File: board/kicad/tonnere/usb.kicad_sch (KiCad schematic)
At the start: 30 parts, among them J19 USB_A, J20 73725-1180RLF, J24 73725-1180RLF, J25 73725-1180RLF, U36 TPD4E02B04DQA, U37 USB2514B_Bi, U38 TPD4E02B04DQA, Y8 24MHz

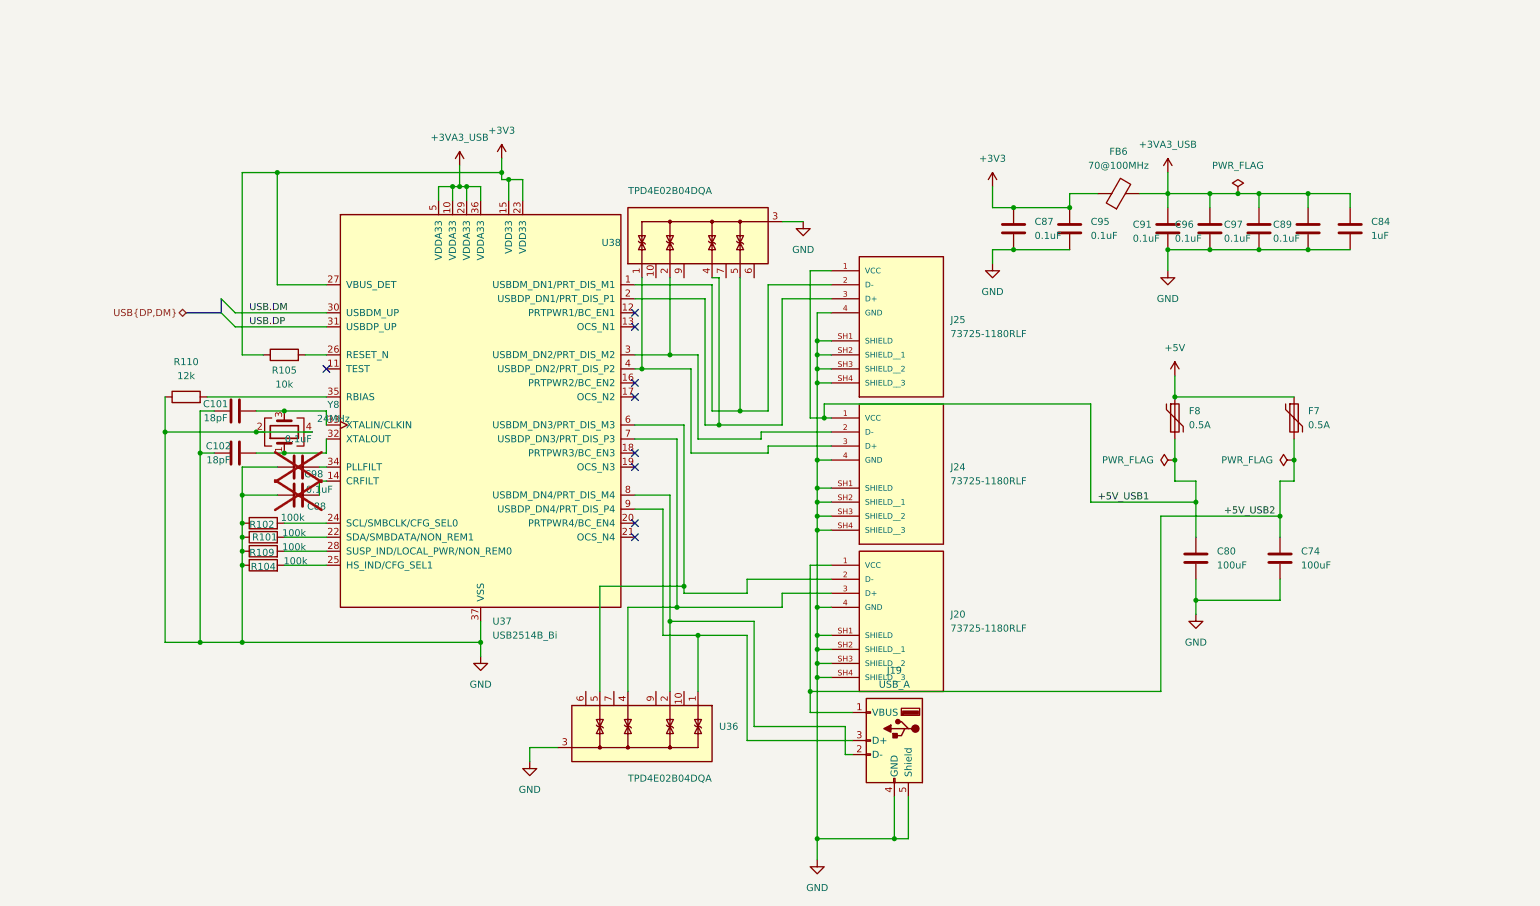
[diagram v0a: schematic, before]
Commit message: 0.60 (not final). Fix errata from 0.51. Added USB2 phy.
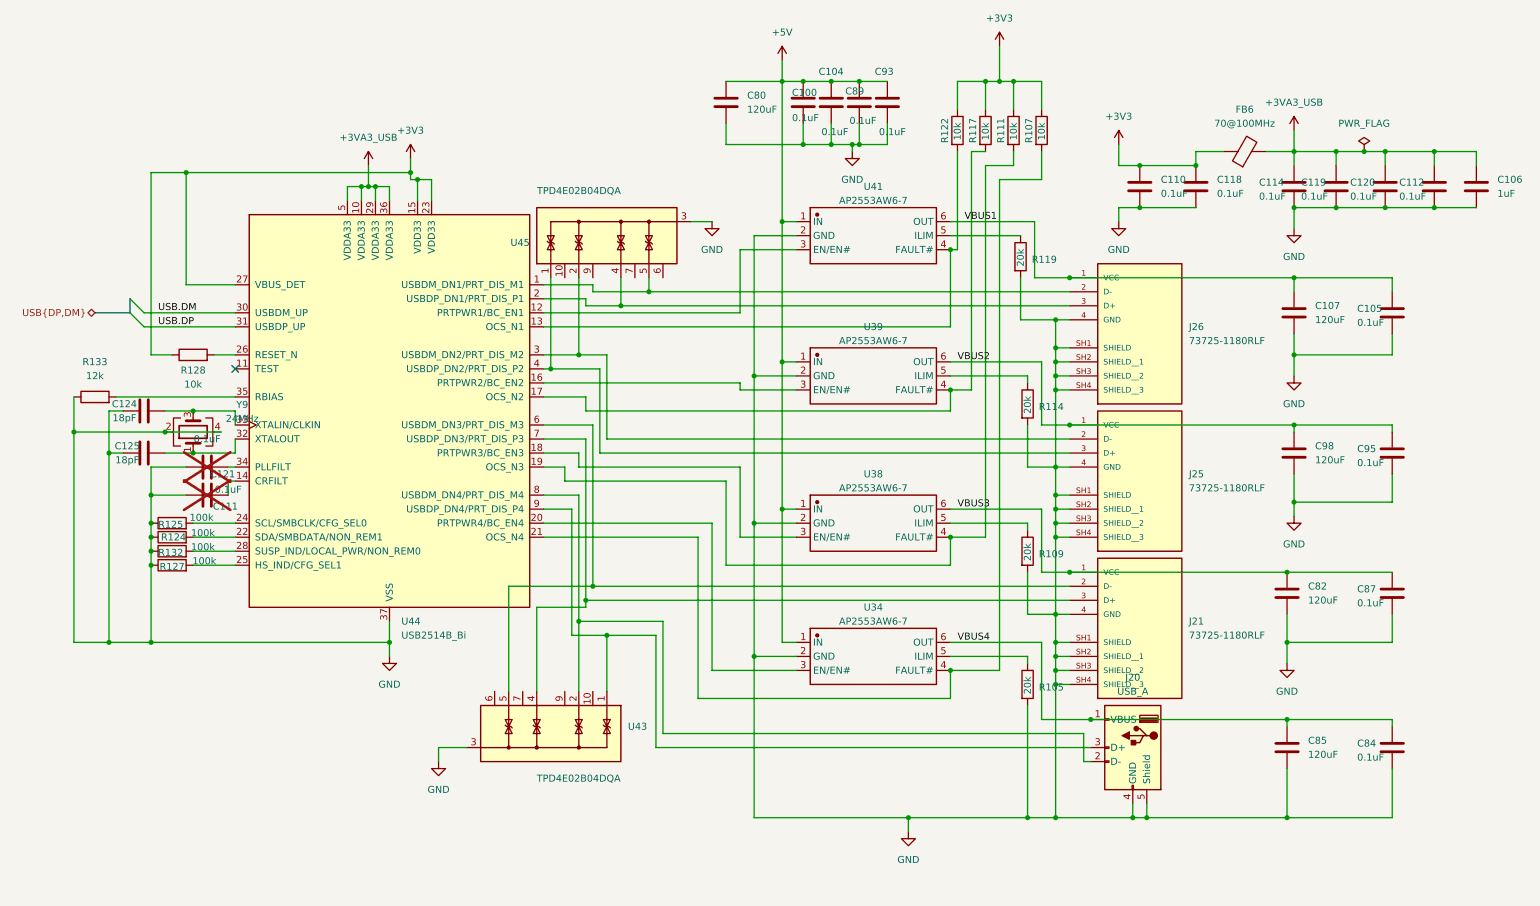
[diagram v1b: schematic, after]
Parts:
- removed C74: 100uF, Capacitor_SMD:C_1206_3216Metric, symbol Device:C
- removed F7, F8: 0.5A, Resistor_SMD:R_0603_1608Metric, symbol Device:Polyfuse
- added C100, C104, C105, C84, C87, C89, C93, C95: 0.1uF, Capacitor_SMD:C_0603_1608Metric, symbol Device:C
- added C107, C82, C85, C98: 120uF, Capacitor_SMD:C_1206_3216Metric, symbol Device:C
- added R105, R109, R114, R119: 20k, Resistor_SMD:R_0603_1608Metric, symbol Device:R
- added R107, R111, R117, R122: 10k, Resistor_SMD:R_0603_1608Metric, symbol Device:R
- added U34, U38, U39, U41: AP2553AW6-7, ap2553:SOT-26_L3.0-W1.6-P0.95-LS2.8-BL, symbol ap2553:AP2553AW6-7
- C80: value 100uF -> 120uF
- renumbered C84 to C106, C87 to C110, C88 to C111, C89 to C112, C91 to C114, C95 to C118, C96 to C119, C97 to C120, C98 to C121, C101 to C124, C102 to C125, J19 to J20, J20 to J21, J24 to J25, J25 to J26, R101 to R124, R102 to R125, R104 to R127, R105 to R128, R109 to R132, R110 to R133, U36 to U43, U37 to U44, U38 to U45, Y8 to Y9
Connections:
- net +3V3: now also R107.1, R111.1, R117.1, R122.1
- net +5V: now also C80.1, C100.1, C104.1, C89.1, C93.1, U34.1 (IN), U38.1 (IN), U39.1 (IN), U41.1 (IN)
- net GND: now also C100.2, C104.2, C105.2, C107.2, C82.2, C84.2, C85.2, C87.2, C89.2, C93.2, C95.2, C98.2, R105.2, R109.2, R114.2, R119.2, U34.2 (GND), U38.2 (GND), U39.2 (GND), U41.2 (GND)
- net at U44.12 (PRTPWR1/BC_EN1): now also U41.3 (EN/EN#)
- net at U44.13 (OCS_N1): now also R122.2, U41.4 (FAULT#)
- net at U44.16 (PRTPWR2/BC_EN2): now also U39.3 (EN/EN#)
- net at U44.17 (OCS_N2): now also R117.2, U39.4 (FAULT#)
- net at U44.18 (PRTPWR3/BC_EN3): now also U38.3 (EN/EN#)
- net at U44.19 (OCS_N3): now also R111.2, U38.4 (FAULT#)
- net at U44.20 (PRTPWR4/BC_EN4): now also U34.3 (EN/EN#)
- net at U44.21 (OCS_N4): now also R107.2, U34.4 (FAULT#)
- removed net +5V_USB1: C80.1, J25.1 (VCC), J26.1 (VCC)
- net +5V_USB2 renamed VBUS3
- net VBUS3: now also C82.1, C87.1, U38.6 (OUT); no longer J20.1 (VBUS)
- new net: R114.1, U39.5 (ILIM)
- new net: R105.1, U34.5 (ILIM)
- new net: R109.1, U38.5 (ILIM)
- new net: R119.1, U41.5 (ILIM)
- new net VBUS1: C105.1, C107.1, J26.1 (VCC), U41.6 (OUT)
- new net VBUS2: C95.1, C98.1, J25.1 (VCC), U39.6 (OUT)
- new net VBUS4: C84.1, C85.1, J20.1 (VBUS), U34.6 (OUT)
- no-connect marks 9 -> 1
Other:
- moved on the sheet: C106, C110, C111, C112, C114, C118, C119, C120, C121, C124, C125, FB6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
